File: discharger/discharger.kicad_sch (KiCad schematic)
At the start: 28 parts, among them J1 XT90, J2 PWR, J3 VOLT, J4 UPDI, J5 UART, Q1 2N7000, Q2 IRF4905, Q3 IRLZ44N, SW1 SW_Push, U1 LM1117-3.3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

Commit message: finish routing and gerbers
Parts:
- removed Q1: 2N7000, Package_TO_SOT_THT:TO-92_Inline, symbol Transistor_FET:2N7000
- added Q1: 2N7002, Package_TO_SOT_SMD:SOT-23, symbol Transistor_FET:2N7002
- added SW1: PRGM/DEBUG, Button_Switch_THT:SW_Slide_1P2T_CK_OS102011MS2Q, symbol Switch:SW_SPDT
- added U3: L7812, symbol Regulator_Linear:L7812
- J1: footprint Connector_AMASS:AMASS_XT60-M_1x02_P7.20mm_Vertical -> discharger:XT90
- J3: footprint Connector_PinHeader_2.54mm:PinHeader_1x03_P2.54mm_Vertical -> discharger:BattMonitor
- J5: value UART -> FAN
- renumbered SW1 to SW2
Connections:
- net +BATT: now also J3.3 (Pin_3); no longer J3.1 (Pin_1)
- net GND: now also J3.1 (Pin_1), Q1.2 (S); no longer J3.3 (Pin_3), J5.3 (Pin_3)
- net TX: now also SW1.3 (C); no longer J5.1 (Pin_1)
- net UPDI: now also SW1.1 (A); no longer J4.1 (Pin_1)
- net at C1.1, D1.1 (K), U1.3 (VI): now also J2.2 (Pin_2); no longer J2.1 (Pin_1)
- net at Q2.2 (D), R10.1, TP1.1: now also U3.1 (IN)
- net at R4.2, R5.1: now also Q1.1 (G)
- net at R8.2: now also Q1.3 (D)
- net +12V: now reaches J5.2 (Pin_2)
- net +12V: now also U3.3 (OUT)
- net at D2.1 (K), Q3.2 (D), TP2.1: now also J5.3 (Pin_3), U3.2 (GND)
- new net: J4.1 (Pin_1), SW1.2 (B)
- no-connect marks 0 -> 1

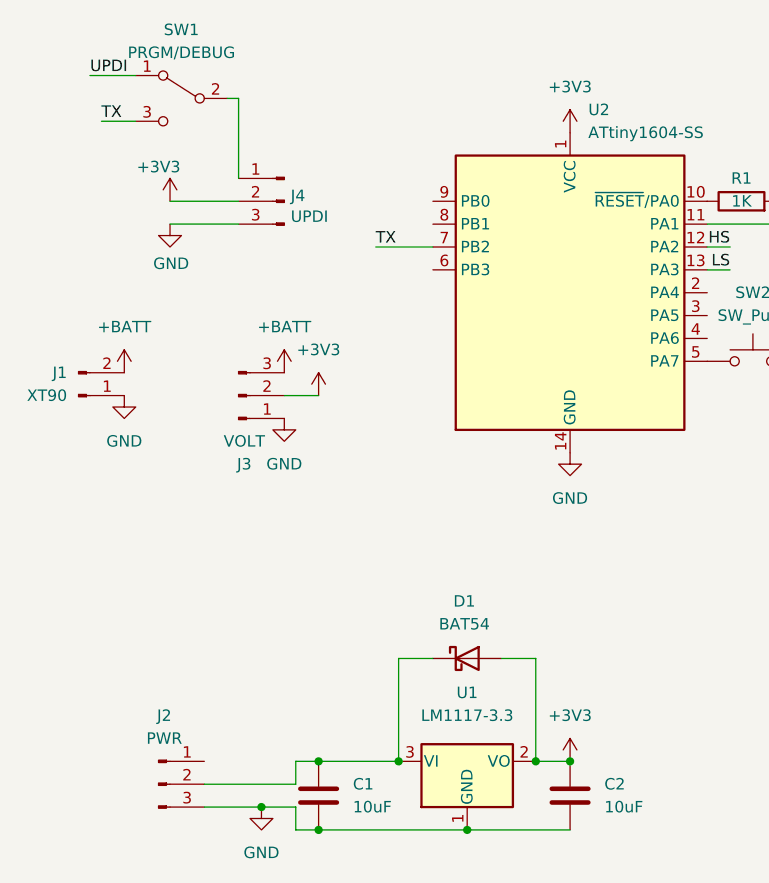
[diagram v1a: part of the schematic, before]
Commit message: 5V instead of 3.3V
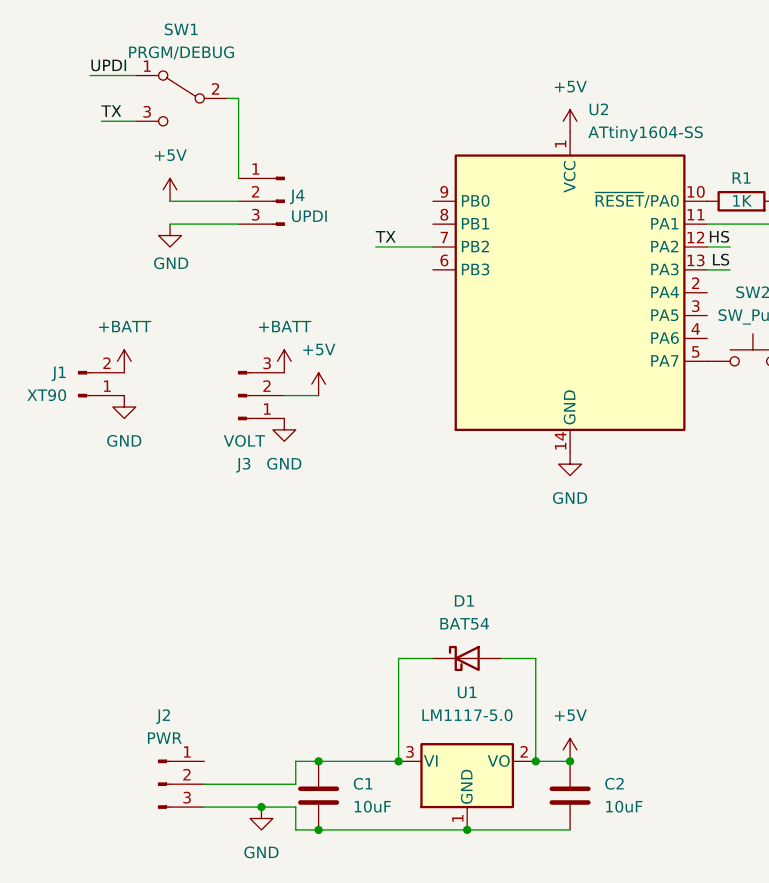
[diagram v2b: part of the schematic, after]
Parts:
- U1: value LM1117-3.3 -> LM1117-5.0
- U3: footprint (none) -> Package_TO_SOT_THT:TO-220-3_Horizontal_TabDown
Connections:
- net +3V3 renamed +5V
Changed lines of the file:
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@@
   (junction (at 207.01 76.2) (diameter 0) (color 0 0 0 0)
   )
+  (junction (at 64.77 101.6) (diameter 0) (color 0 0 0 0)
+  )
+  (junction (at 190.5 76.2) (diameter 0) (color 0 0 0 0)
+  )
+  (junction (at 163.83 52.07) (diameter 0) (color 0 0 0 0)
+  )
+  (junction (at 87.63 104.14) (diameter 0) (color 0 0 0 0)
+  )
+  (junction (at 138.43 44.45) (diameter 0) (color 0 0 0 0)
+  )
   (junction (at 99.06 96.52) (diameter 0) (color 0 0 0 0)
-  )
-  (junction (at 64.77 101.6) (diameter 0) (color 0 0 0 0)
-  )
-  (junction (at 190.5 76.2) (diameter 0) (color 0 0 0 0)
-  )
-  (junction (at 163.83 52.07) (diameter 0) (color 0 0 0 0)
-  )
-  (junction (at 87.63 104.14) (diameter 0) (color 0 0 0 0)
-  )
-  (junction (at 138.43 44.45) (diameter 0) (color 0 0 0 0)
   )
   (junction (at 163.83 72.39) (diameter 0) (color 0 0 0 0)
@@
     (effects (font (size 1.27 1.27)) (justify left bottom))
   )
+  (symbol (lib_id "power:+5V") (at 71.12 55.88 0) (unit 1)
+    (in_bom yes) (on_board yes) (fields_autoplaced)
+    (property "Reference" "#PWR?" (id 0) (at 71.12 59.69 0)
+      (effects (font (size 1.27 1.27)) hide)
+    )
+    (property "Value" "+5V" (id 1) (at 71.12 50.8 0))
+    (property "Footprint" "" (id 2) (at 71.12 55.88 0)
+      (effects (font (size 1.27 1.27)) hide)
+    )
+    (property "Datasheet" "" (id 3) (at 71.12 55.88 0)
+      (effects (font (size 1.27 1.27)) hide)
+    )
+    (pin "1")
+  )
   (symbol (lib_id "Regulator_Linear:LM1117-3.3") (at 87.63 96.52 0) (unit 1)
     (in_bom yes) (on_board yes) (fields_autoplaced)
     (property "Reference" "U1" (id 0) (at 87.63 88.9 0))
-    (property "Value" "LM1117-3.3" (id 1) (at 87.63 91.44 0))
+    (property "Value" "LM1117-5.0" (id 1) (at 87.63 91.44 0))
     (property "Footprint" "Package_TO_SOT_SMD:SOT-223-3_TabPin2" (id 2) (at 87.63 96.52 0)
       (effects (font (size 1.27 1.27)) hide)
@@
     (pin "2")
   )
-  (symbol (lib_id "power:+3V3") (at 71.12 55.88 0) (unit 1)
-    (in_bom yes) (on_board yes) (fields_autoplaced)
-    (property "Reference" "#PWR08" (id 0) (at 71.12 59.69 0)
-      (effects (font (size 1.27 1.27)) hide)
-    )
-    (property "Value" "+3V3" (id 1) (at 71.12 50.8 0))
-    (property "Footprint" "" (id 2) (at 71.12 55.88 0)
-      (effects (font (size 1.27 1.27)) hide)
-    )
-    (property "Datasheet" "" (id 3) (at 71.12 55.88 0)
-      (effects (font (size 1.27 1.27)) hide)
-    )
-    (pin "1")
-  )
-  (symbol (lib_id "power:+3V3") (at 99.06 96.52 0) (unit 1)
-    (in_bom yes) (on_board yes) (fields_autoplaced)
-    (property "Reference" "#PWR011" (id 0) (at 99.06 100.33 0)
-      (effects (font (size 1.27 1.27)) hide)
-    )
-    (property "Value" "+3V3" (id 1) (at 99.06 91.44 0))
+  (symbol (lib_id "power:+5V") (at 99.06 96.52 0) (unit 1)
+    (in_bom yes) (on_board yes) (fields_autoplaced)
+    (property "Reference" "#PWR?" (id 0) (at 99.06 100.33 0)
+      (effects (font (size 1.27 1.27)) hide)
+    )
+    (property "Value" "+5V" (id 1) (at 99.06 91.44 0))
     (property "Footprint" "" (id 2) (at 99.06 96.52 0)
       (effects (font (size 1.27 1.27)) hide)
@@
     (pin "1")
   )
+  (symbol (lib_id "power:+5V") (at 54.61 34.29 0) (unit 1)
+    (in_bom yes) (on_board yes) (fields_autoplaced)
+    (property "Reference" "#PWR?" (id 0) (at 54.61 38.1 0)
+      (effects (font (size 1.27 1.27)) hide)
+    )
+    (property "Value" "+5V" (id 1) (at 54.61 29.21 0))
+    (property "Footprint" "" (id 2) (at 54.61 34.29 0)
+      (effects (font (size 1.27 1.27)) hide)
+    )
+    (property "Datasheet" "" (id 3) (at 54.61 34.29 0)
+      (effects (font (size 1.27 1.27)) hide)
+    )
+    (pin "1")
+  )
   (symbol (lib_id "Device:C") (at 128.27 40.64 0) (unit 1)
     (in_bom yes) (on_board yes) (fields_autoplaced)
@@
     (property "Reference" "U3" (id 0) (at 207.01 49.53 0))
     (property "Value" "L7812" (id 1) (at 207.01 52.07 0))
-    (property "Footprint" "" (id 2) (at 207.645 60.96 0)
+    (property "Footprint" "Package_TO_SOT_THT:TO-220-3_Horizontal_TabDown" (id 2) (at 207.645 60.96 0)
       (effects (font (size 1.27 1.27) italic) (justify left) hide)
     )
@@
     (pin "2")
     (pin "3")
-  )
-  (symbol (lib_id "power:+3V3") (at 54.61 34.29 0) (unit 1)
-    (in_bom yes) (on_board yes)
-    (property "Reference" "#PWR03" (id 0) (at 54.61 38.1 0)
-      (effects (font (size 1.27 1.27)) hide)
-    )
-    (property "Value" "+3V3" (id 1) (at 53.34 30.48 0))
-    (property "Footprint" "" (id 2) (at 54.61 34.29 0)
-      (effects (font (size 1.27 1.27)) hide)
-    )
-    (property "Datasheet" "" (id 3) (at 54.61 34.29 0)
-      (effects (font (size 1.27 1.27)) hide)
-    )
-    (pin "1")
   )
   (symbol (lib_id "Device:R") (at 158.75 81.28 90) (unit 1)
@@
     (pin "1")
     (pin "2")
-  )
-  (symbol (lib_id "power:+3V3") (at 99.06 26.67 0) (unit 1)
-    (in_bom yes) (on_board yes) (fields_autoplaced)
-    (property "Reference" "#PWR09" (id 0) (at 99.06 30.48 0)
-      (effects (font (size 1.27 1.27)) hide)
-    )
-    (property "Value" "+3V3" (id 1) (at 99.06 21.59 0))
-    (property "Footprint" "" (id 2) (at 99.06 26.67 0)
-      (effects (font (size 1.27 1.27)) hide)
-    )
-    (property "Datasheet" "" (id 3) (at 99.06 26.67 0)
-      (effects (font (size 1.27 1.27)) hide)
-    )
-    (pin "1")
   )
   (symbol (lib_id "Transistor_FET:IRF4905") (at 171.45 52.07 0) (mirror x) (unit 1)
@@
     (pin "2")
   )
+  (symbol (lib_id "power:+5V") (at 99.06 26.67 0) (unit 1)
+    (in_bom yes) (on_board yes) (fields_autoplaced)
+    (property "Reference" "#PWR?" (id 0) (at 99.06 30.48 0)
+      (effects (font (size 1.27 1.27)) hide)
+    )
+    (property "Value" "+5V" (id 1) (at 99.06 21.59 0))
+    (property "Footprint" "" (id 2) (at 99.06 26.67 0)
+      (effects (font (size 1.27 1.27)) hide)
+    )
+    (property "Datasheet" "" (id 3) (at 99.06 26.67 0)
+      (effects (font (size 1.27 1.27)) hide)
+    )
+    (pin "1")
+  )
   (symbol (lib_id "Device:R") (at 153.67 68.58 0) (unit 1)
     (in_bom yes) (on_board yes)
@@
       (reference "#PWR02") (unit 1) (value "GND") (footprint "")
     )
-    (path "/5c24a5da-9fa7-4ca3-ad0b-058d0775f648"
-      (reference "#PWR03") (unit 1) (value "+3V3") (footprint "")
-    )
     (path "/f407b4da-c39a-4e33-af72-13358936b134"
       (reference "#PWR04") (unit 1) (value "GND") (footprint "")
@@
       (reference "#PWR07") (unit 1) (value "GND") (footprint "")
     )
-    (path "/096f638a-4c7c-4fba-bf3f-287a04bf902e"
-      (reference "#PWR08") (unit 1) (value "+3V3") (footprint "")
-    )
-    (path "/91ea9d4c-698b-41a1-b067-9c5c68e0ee17"
-      (reference "#PWR09") (unit 1) (value "+3V3") (footprint "")
-    )
     (path "/141dee05-3ef1-49f3-860f-62ee438317b6"
       (reference "#PWR010") (unit 1) (value "GND") (footprint "")
     )
-    (path "/0fea8e56-3ea2-489a-8dae-e15bd3b8240b"
-      (reference "#PWR011") (unit 1) (value "+3V3") (footprint "")
-    )
     (path "/d5d6ea53-0789-4b1d-b01b-985d59a4293d"
       (reference "#PWR012") (unit 1) (value "GND") (footprint "")
@@
       (reference "#PWR018") (unit 1) (value "+12V") (footprint "")
     )
+    (path "/0203321a-624c-4d8f-b13c-f7bdeef4f332"
+      (reference "#PWR?") (unit 1) (value "+5V") (footprint "")
+    )
+    (path "/088f73d1-3e9f-4dc3-8fec-fd7eac667c90"
+      (reference "#PWR?") (unit 1) (value "+5V") (footprint "")
+    )
+    (path "/57a80c68-8ebe-4900-9289-3287b226cb80"
+      (reference "#PWR?") (unit 1) (value "+5V") (footprint "")
+    )
+    (path "/eab8ecb6-a9ff-41b6-b8f5-bf155f72f332"
+      (reference "#PWR?") (unit 1) (value "+5V") (footprint "")
+    )
     (path "/e76f0462-347a-4895-8e60-aa36363d8dc4"
       (reference "C1") (unit 1) (value "10uF") (footprint "Capacitor_SMD:C_0805_2012Metric")
@@
     )
     (path "/0409f65b-dab1-4650-9050-d208a9fff552"
-      (reference "U1") (unit 1) (value "LM1117-3.3") (footprint "Package_TO_SOT_SMD:SOT-223-3_TabPin2")
+      (reference "U1") (unit 1) (value "LM1117-5.0") (footprint "Package_TO_SOT_SMD:SOT-223-3_TabPin2")
     )
     (path "/c3da5622-bcbb-4c99-895c-80542b5542bf"
